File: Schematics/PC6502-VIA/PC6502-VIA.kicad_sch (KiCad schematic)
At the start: 38 parts, among them J1 BUS, J2 Conn_02x06_Odd_Even, J3 Conn_02x06_Odd_Even, J4 Conn_02x04_Odd_Even, J5 Conn_02x04_Odd_Even, J6 Conn_02x06_Odd_Even, J7 Conn_02x06_Odd_Even, J8 Conn_02x05_Odd_Even, U1 W65C22NxP, U2 W65C22NxP, U4 ATF1502AS

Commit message: Add Power/Storage PCB
Also tidied template
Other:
- note added: "I now realise that some peripherals need the stretched CPU clock, DOH! So I'll mod wire the CPU_CLOCK on the main CPU board to SP_CLK :("
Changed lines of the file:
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@@
+		)
+	)
+	(text "I now realise that some peripherals \nneed the stretched CPU clock, DOH!\nSo I'll mod wire the CPU_CLOCK on \nthe main CPU board to SP_CLK :("
+		(exclude_from_sim no)
+		(at 35.56 174.244 0)
+		(effects
+			(font
+				(size 1.27 1.27)
+			)
 		)
 	)

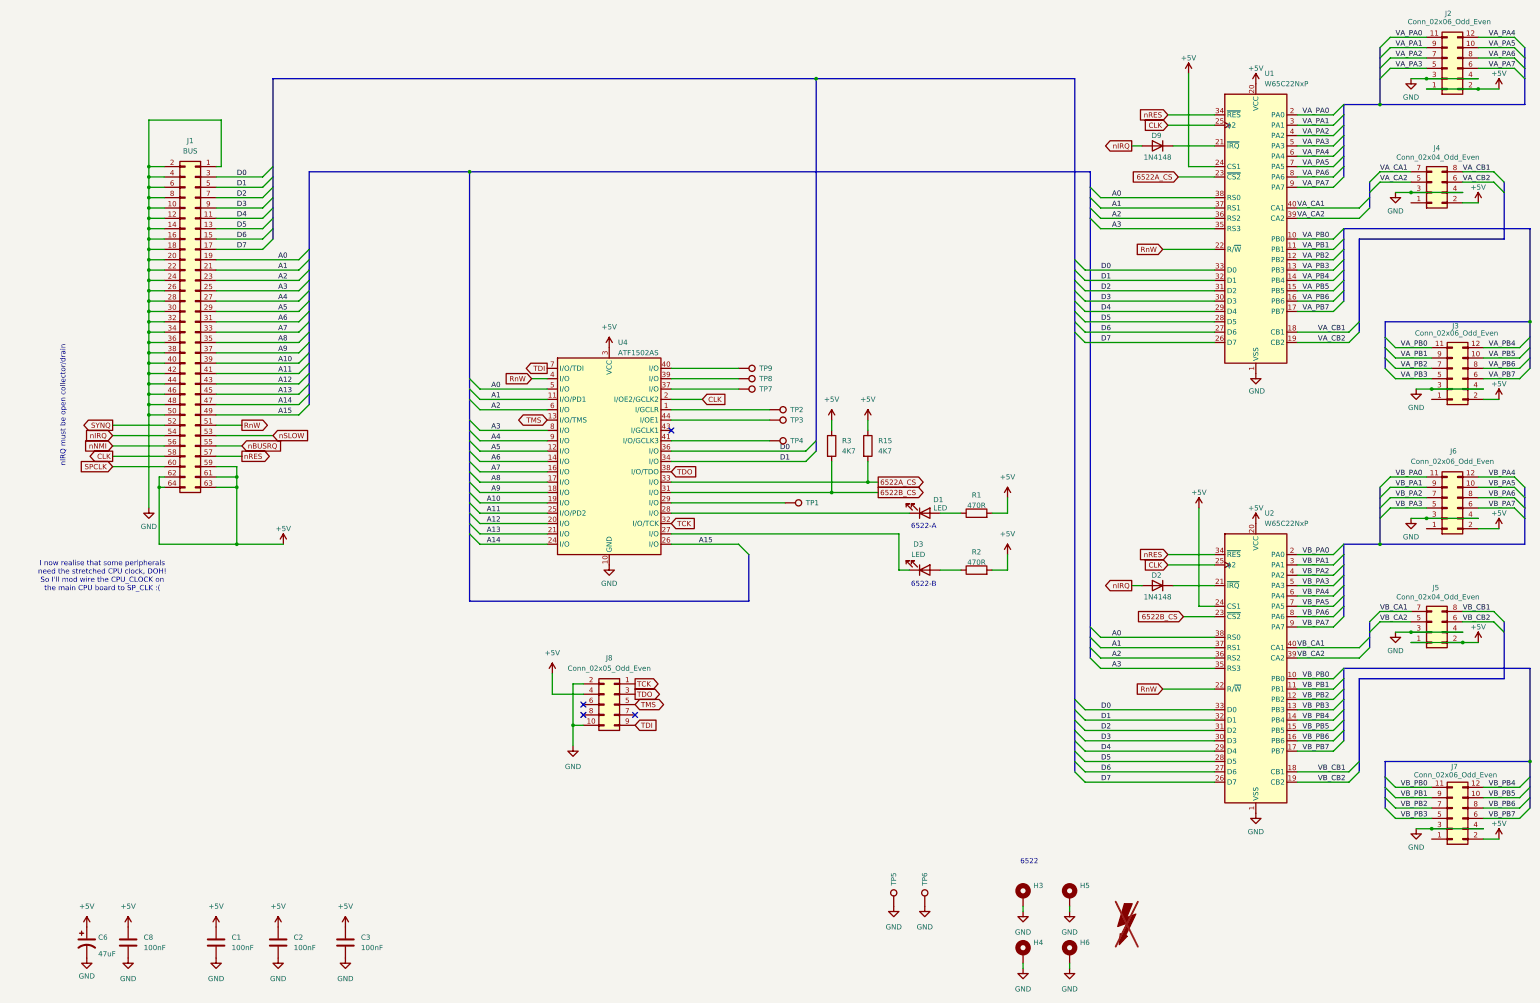
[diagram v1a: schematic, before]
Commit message: V1.1 CPU, VIA and POWER PCBs uploaded
A simpler CPU board (direct link to FT245R, 74161 removed and some tidying of tracks). Fixed a couple of floating inputs to RAM/ROM
VIA is much simpler, having just the one VIA chip.
POWER board has USB-PD and a 24VDC input for higher power stuff in the future.
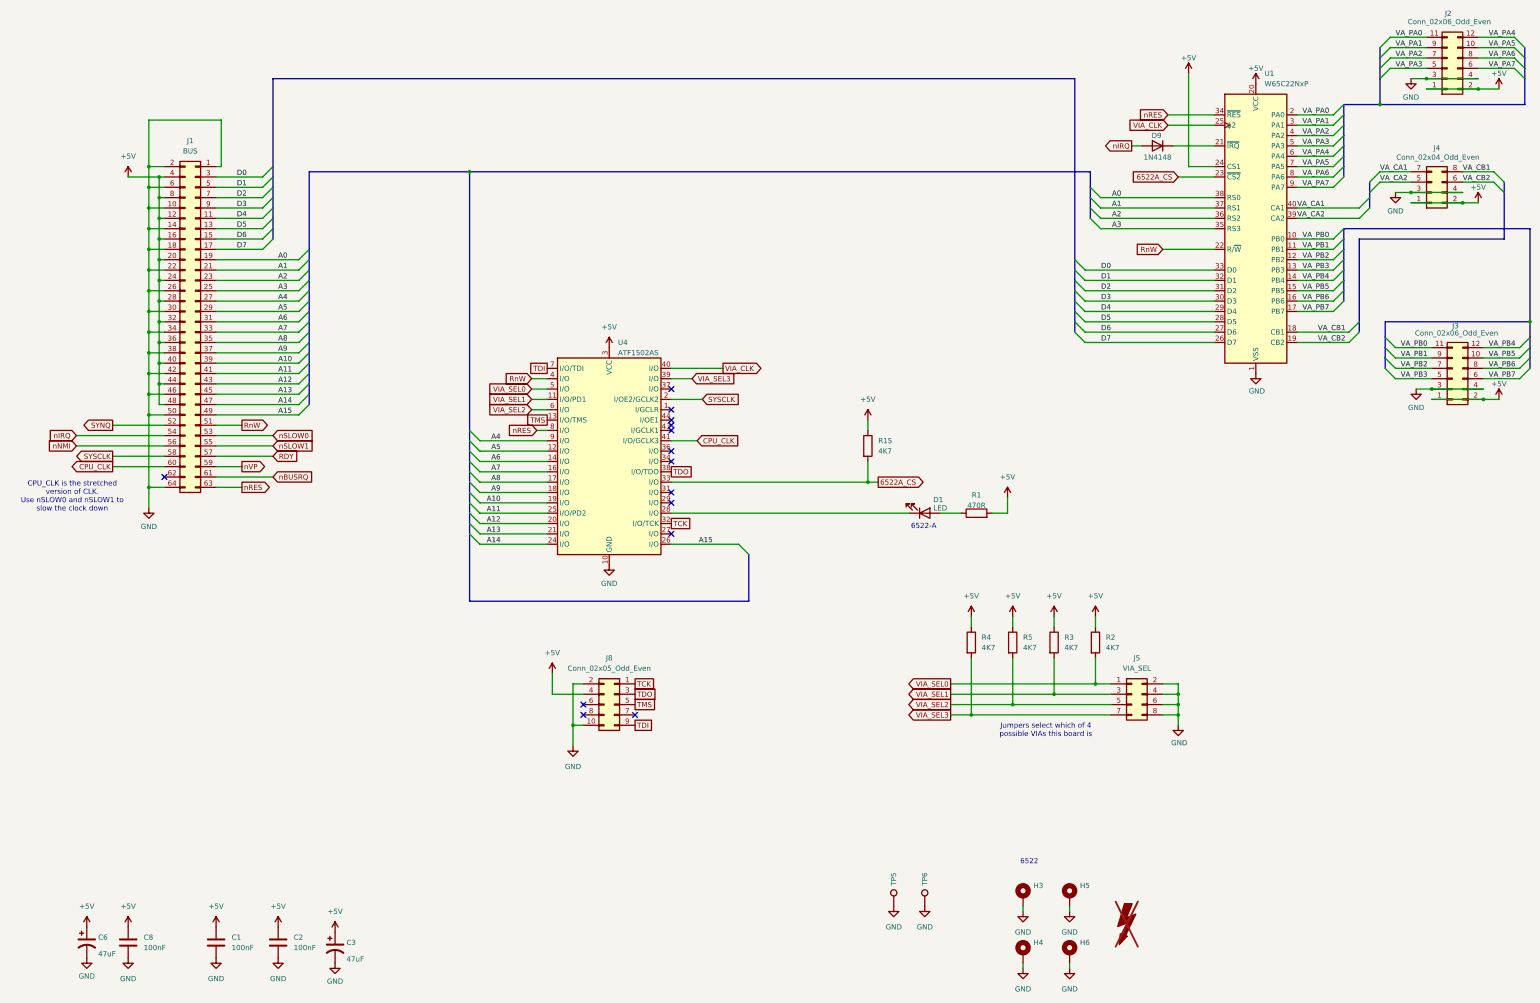
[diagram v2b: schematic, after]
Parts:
- removed C3: 100nF, Capacitor_SMD:C_0805_2012Metric, symbol Device:C
- removed D2: 1N4148, Diode_THT:D_DO-35_SOD27_P7.62mm_Horizontal, symbol Diode:1N4148
- removed D3: LED, LTL-4221NHBP:LTL4221NHBP, symbol Device:LED
- removed J6, J7: Conn_02x06_Odd_Even, Connector_PinSocket_2.54mm:PinSocket_2x06_P2.54mm_Horizontal, symbol Connector_Generic:Conn_02x06_Odd_Even
- removed TP1, TP2, TP3, TP4, TP7, TP8, TP9: TestPoint, TestPoint:TestPoint_Loop_D1.80mm_Drill1.0mm_Beaded, symbol Connector:TestPoint
- removed U2: W65C22NxP, Package_DIP:DIP-40_W15.24mm, symbol 65xx-library:W65C22NxP
- added C3: 47uF, Capacitor_SMD:C_1206_3216Metric, symbol Device:C_Polarized_US
- added R4, R5: 4K7, Resistor_SMD:R_0603_1608Metric_Pad0.98x0.95mm_HandSolder, symbol Device:R
- J5: value Conn_02x04_Odd_Even -> VIA_SEL; footprint Connector_PinSocket_2.54mm:PinSocket_2x04_P2.54mm_Horizontal -> Connector_PinHeader_2.54mm:PinHeader_2x04_P2.54mm_Horizontal
- R2: value 470R -> 4K7
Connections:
- net SPCLK is gone; now on net CPU_CLK: J1.60 (Pin_60)
- net VB_CA1 is gone; now on net VIA_SEL3: J5.7 (Pin_7)
- net VB_CB1 is gone; now on net GND: J5.8 (Pin_8)
- net VB_CB2 is gone; now on net GND: J5.6 (Pin_6)
- net +5V: now also J1.12 (Pin_12), J1.16 (Pin_16), J1.20 (Pin_20), J1.24 (Pin_24), J1.28 (Pin_28), J1.32 (Pin_32), J1.36 (Pin_36), J1.4 (Pin_4), J1.40 (Pin_40), J1.44 (Pin_44), J1.48 (Pin_48), J1.8 (Pin_8), J3.1 (Pin_1), J4.1 (Pin_1), R2.1, C3.1, R4.1, R5.1; no longer J1.59 (Pin_59), J1.61 (Pin_61), J1.62 (Pin_62), J1.63 (Pin_63), J1.64 (Pin_64), J5.1 (Pin_1), J5.2 (Pin_2), R2.2
- net A0: no longer U4.5 (I/O)
- net A1: no longer U4.11 (I/O/PD1)
- net A2: no longer U4.6 (I/O)
- net A3: no longer U4.8 (I/O)
- net D0: no longer U4.36 (I/O)
- net D1: no longer U4.34 (I/O)
- net GND: now also J1.64 (Pin_64), J5.2 (Pin_2), C3.2; no longer J1.12 (Pin_12), J1.16 (Pin_16), J1.20 (Pin_20), J1.24 (Pin_24), J1.28 (Pin_28), J1.32 (Pin_32), J1.36 (Pin_36), J1.4 (Pin_4), J1.40 (Pin_40), J1.44 (Pin_44), J1.48 (Pin_48), J1.8 (Pin_8), J5.3 (Pin_3)
- net nBUSRQ: now also J1.61 (Pin_61); no longer J1.55 (Pin_55)
- net nRES: now also J1.63 (Pin_63), U4.8 (I/O); no longer J1.57 (Pin_57)
- net VIA_SEL3: now reaches U4.39 (I/O)
- net VIA_SEL3: now also R4.2
- net VIA_CLK: now reaches U4.40 (I/O)
- net VIA_CLK: now also U1.25 (ϕ2)
- net CPU_CLK: now reaches U4.41 (I/O/GCLK3)
- net 6522B_CS: no longer names the net of U4.31 (I/O)
- net 6522B_CS: no longer R3.2
- net CLK renamed SYSCLK
- net SYSCLK: no longer U1.25 (ϕ2)
- net VB_CA2 renamed VIA_SEL2
- net VIA_SEL2: now also U4.6 (I/O), R5.2
- net nSLOW renamed nSLOW0
- new net RDY: J1.57 (Pin_57)
- new net VIA_SEL0: J5.1 (Pin_1), R2.2, U4.5 (I/O)
- new net VIA_SEL1: J5.3 (Pin_3), R3.2, U4.11 (I/O/PD1)
- new net nSLOW1: J1.55 (Pin_55)
- new net nVP: J1.59 (Pin_59)
- no-connect marks 4 -> 14
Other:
- note added: "CPU_CLK is the stretched version of CLK. Use nSLOW0 and nSLOW1 to slow the clock down"
- note added: "Jumpers select which of 4 possible VIAs this board is"
- note removed: "6522-B"
- note removed: "I now realise that some peripherals need the stretched CPU clock, DOH! So I'll mod wire the CPU_CLOCK on the main CPU board to SP_CLK :("
- note removed: "nIRQ must be open collector/drain"
